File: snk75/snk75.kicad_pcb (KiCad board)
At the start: 2 copper layers, 274 parts, among them J1 USB_C_Receptacle_USB2.0, U1 ATmega32U4-AU, Y1 16MHZ

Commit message: Added PCB rounded borders
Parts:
- D15: moved to F.Cu
- moved R12 471.7 mm to (66.7, 174.4)
- moved R16 471.7 mm to (66.7, 181.0)
- moved R20 471.7 mm to (72.6, 177.7)
- moved R23 471.7 mm to (72.6, 184.3)
- moved R27 471.7 mm to (66.7, 177.7)
- moved R54 471.7 mm to (66.7, 167.8)
- moved R56 471.7 mm to (72.6, 181.0)
- moved R76 471.7 mm to (66.7, 171.1)
- moved R81 471.7 mm to (72.6, 167.8)
- moved R87 471.7 mm to (72.6, 174.4)
- moved R9 471.7 mm to (72.6, 171.1)
- moved R10 410.7 mm to (29.8, 181.3)
- moved R13 410.7 mm to (29.8, 174.7)
- moved R15 410.7 mm to (23.8, 178.0)
- moved R24 410.7 mm to (29.8, 168.2)
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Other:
- board outline added: 314.3 x 123.8 mm

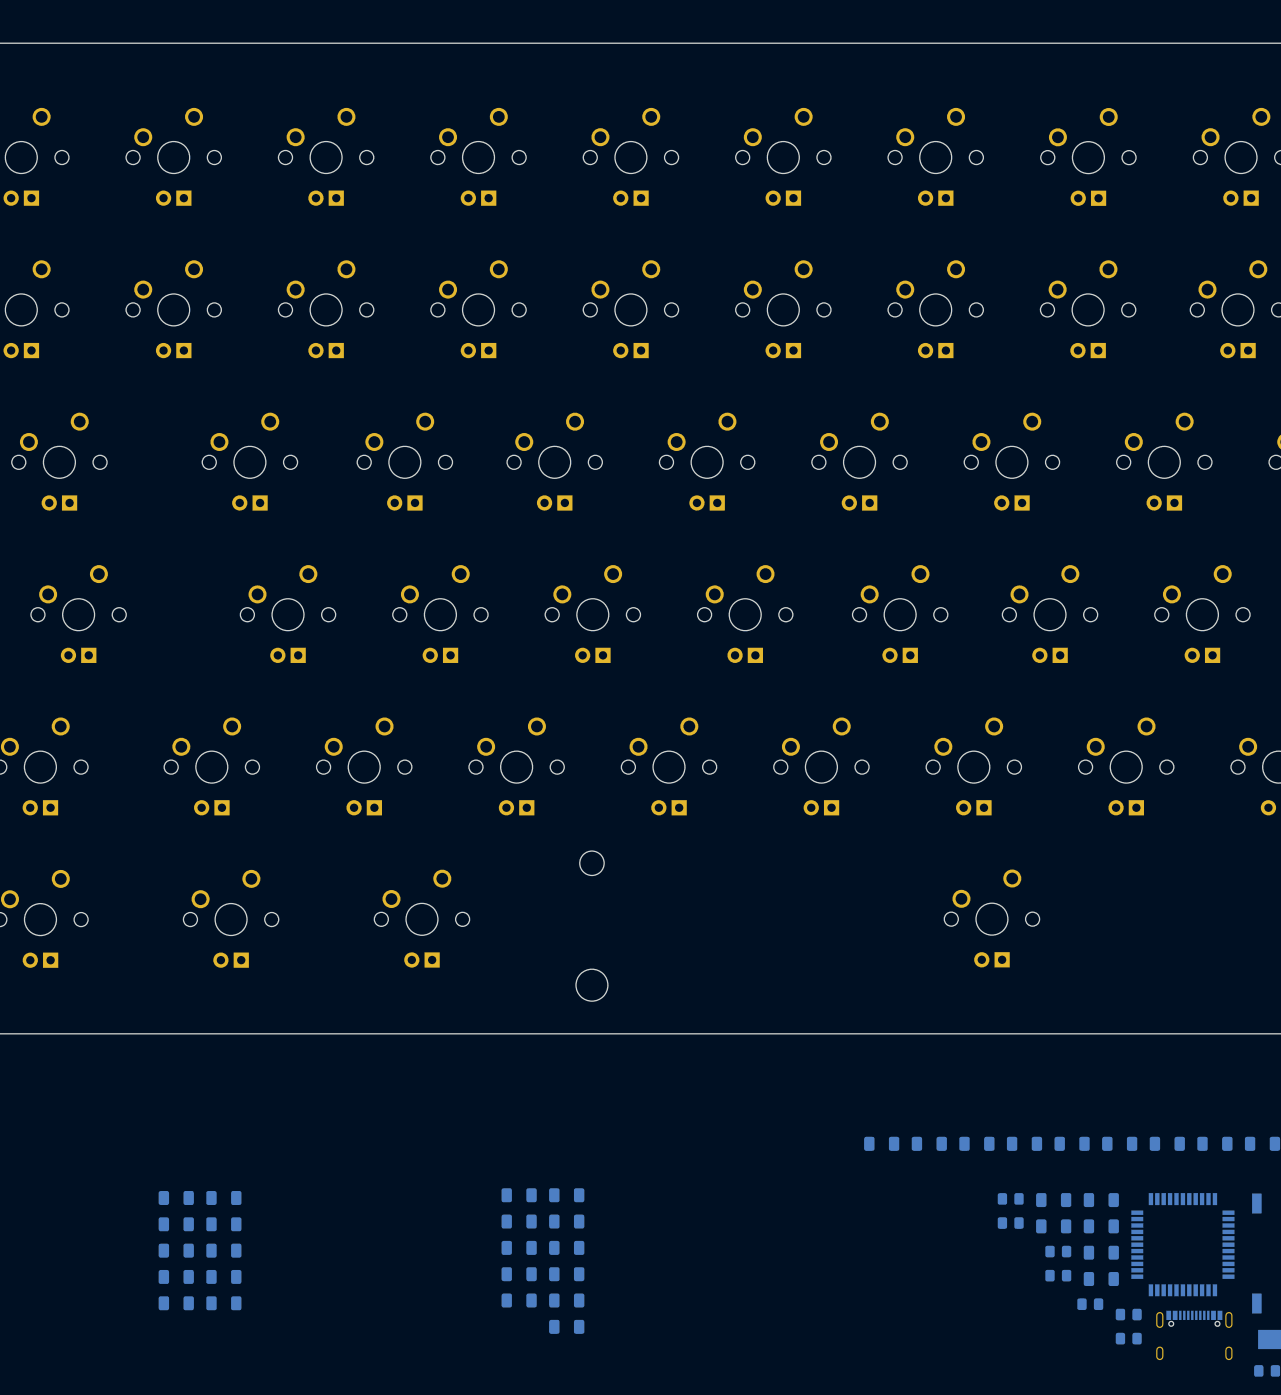
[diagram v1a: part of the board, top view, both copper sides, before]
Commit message: Fixed reset
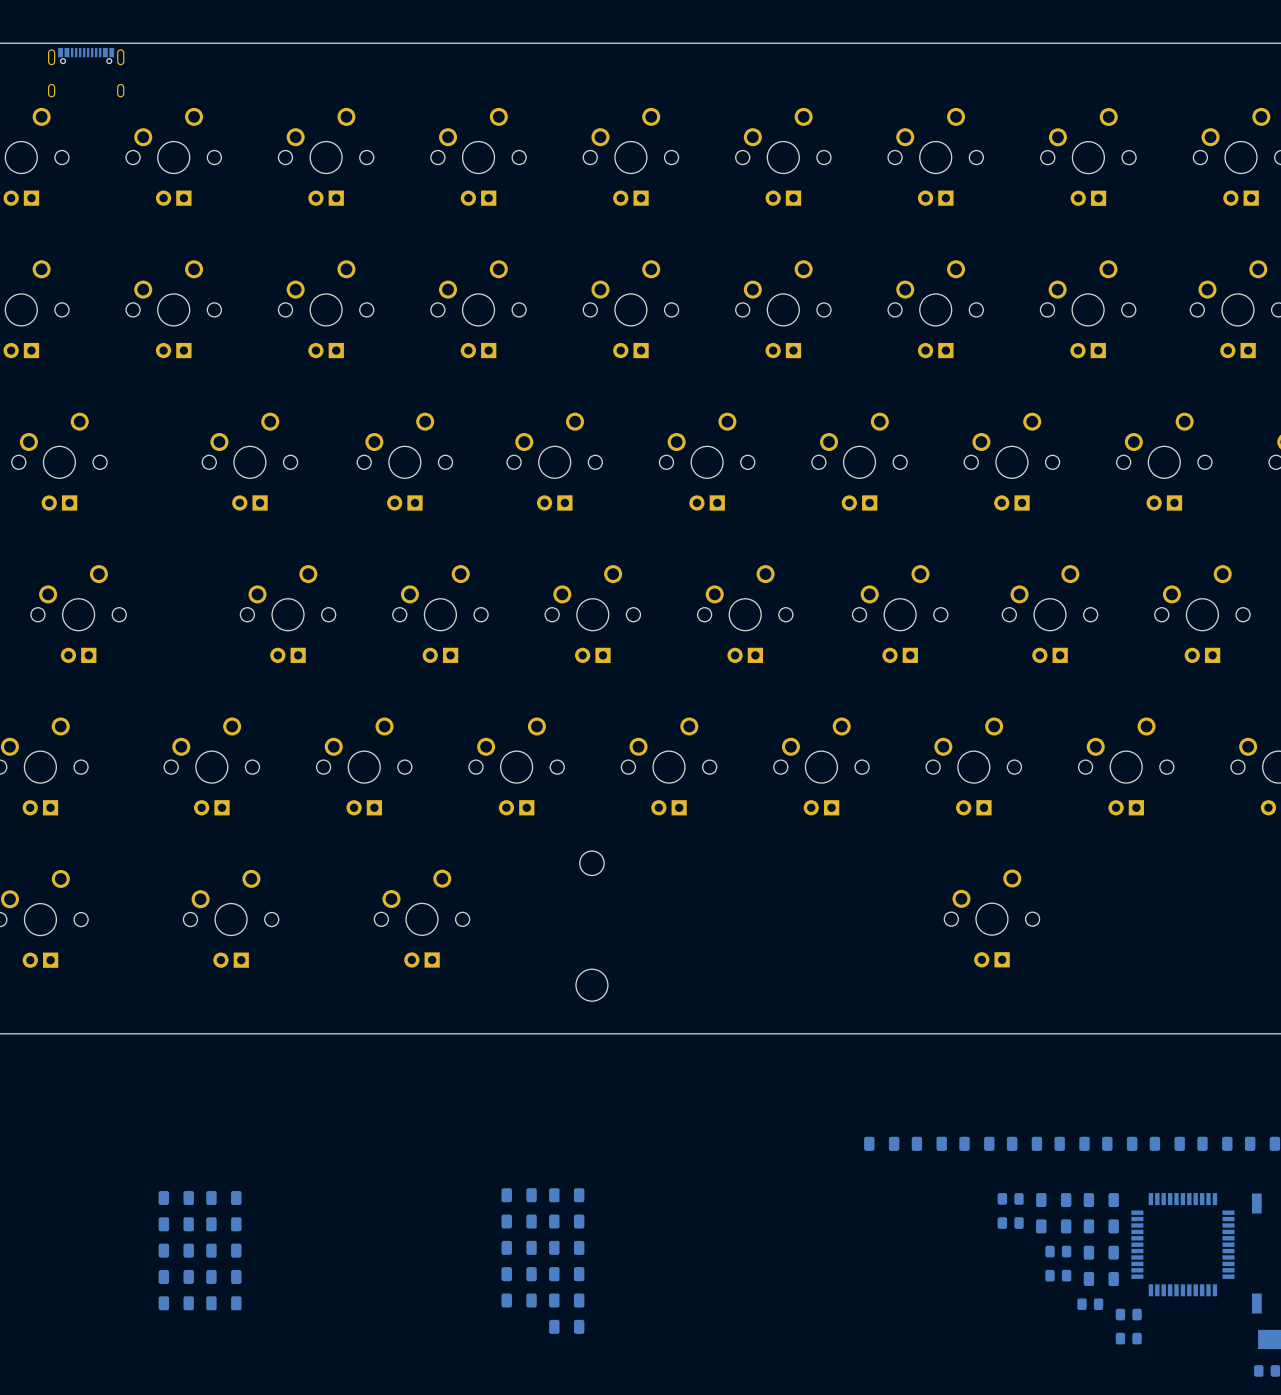
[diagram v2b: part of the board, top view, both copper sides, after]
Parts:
- moved J1 210.0 mm to (12.6, 27.5)
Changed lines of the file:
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@@
   )
   (footprint "Connector_USB:USB_C_Receptacle_Palconn_UTC16-G" (layer "B.Cu")
-    (at 151.075 185.3375 180)
+    (at 12.55 27.5 180)
     (descr "http://www.palpilot.com/wp-content/uploads/2017/05/UTC027-GKN-OR-Rev-A.pdf")
     (tags "USB C Type-C Receptacle USB2.0")

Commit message: Began routing
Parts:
- removed 1uF1: C?, Capacitor_SMD:C_0805_2012Metric_Pad1.18x1.45mm_HandSolder
- added C10: 100n, Capacitor_SMD:C_0805_2012Metric_Pad1.18x1.45mm_HandSolder, B.Cu at (143.8, 138.8)
- added C11: 100nF, Capacitor_SMD:C_0805_2012Metric_Pad1.18x1.45mm_HandSolder, F.Cu at (78.8, -18.6)
- added C12: 100nF, Capacitor_SMD:C_0805_2012Metric_Pad1.18x1.45mm_HandSolder, F.Cu at (101.8, -28.0)
- added C13: 100nF, Capacitor_SMD:C_0805_2012Metric_Pad1.18x1.45mm_HandSolder, F.Cu at (106.7, -37.0)
- added C14: 100nF, Capacitor_SMD:C_0805_2012Metric_Pad1.18x1.45mm_HandSolder, F.Cu at (114.8, -43.1)
- added C15: 100nF, Capacitor_SMD:C_0805_2012Metric_Pad1.18x1.45mm_HandSolder, F.Cu at (101.8, -31.0)
- added C16: 100nF, Capacitor_SMD:C_0805_2012Metric_Pad1.18x1.45mm_HandSolder, F.Cu at (83.6, -18.6)
- added C17: 100nF, Capacitor_SMD:C_0805_2012Metric_Pad1.18x1.45mm_HandSolder, F.Cu at (101.8, -34.0)
- added C18: 100nF, Capacitor_SMD:C_0805_2012Metric_Pad1.18x1.45mm_HandSolder, F.Cu at (74.0, -18.6)
- added C19: 100nF, Capacitor_SMD:C_0805_2012Metric_Pad1.18x1.45mm_HandSolder, F.Cu at (93.7, -21.7)
- added C20: 100nF, Capacitor_SMD:C_0805_2012Metric_Pad1.18x1.45mm_HandSolder, F.Cu at (110.0, -43.1)
- added C21: 100nF, Capacitor_SMD:C_0805_2012Metric_Pad1.18x1.45mm_HandSolder, F.Cu at (69.2, -18.6)
- added C22: 100nF, Capacitor_SMD:C_0805_2012Metric_Pad1.18x1.45mm_HandSolder, F.Cu at (106.7, -34.0)
- added C23: 100nF, Capacitor_SMD:C_0805_2012Metric_Pad1.18x1.45mm_HandSolder, F.Cu at (101.8, -37.0)
- added C24: 100nF, Capacitor_SMD:C_0805_2012Metric_Pad1.18x1.45mm_HandSolder, F.Cu at (93.7, -24.8)
- added C25: 100nF, Capacitor_SMD:C_0805_2012Metric_Pad1.18x1.45mm_HandSolder, F.Cu at (110.0, -40.1)
- added C26: 100nF, Capacitor_SMD:C_0805_2012Metric_Pad1.18x1.45mm_HandSolder, F.Cu at (135.2, 175.0)
- added C27: 100nF, Capacitor_SMD:C_0805_2012Metric_Pad1.18x1.45mm_HandSolder, F.Cu at (135.2, 169.5)
- added C8: 100n, Capacitor_SMD:C_0805_2012Metric_Pad1.18x1.45mm_HandSolder, B.Cu at (148.3, 125.0)
- added C9: 1u, Capacitor_SMD:C_0805_2012Metric_Pad1.18x1.45mm_HandSolder, B.Cu at (143.3, 130.0)
- added D100: SK6812MINI-E, acheron_Components:SK6812MINI_3535_6028_3.2x2.8mm_Round, F.Cu at (87.2, -41.6)
- added D101: SK6812MINI-E, acheron_Components:SK6812MINI_3535_6028_3.2x2.8mm_Round, F.Cu at (70.9, -29.3)
- added D86: SK6812MINI-E, acheron_Components:SK6812MINI_3535_6028_3.2x2.8mm_Round, F.Cu at (79.0, -23.2)
- added D87: SK6812MINI-E, acheron_Components:SK6812MINI_3535_6028_3.2x2.8mm_Round, F.Cu at (79.0, -29.3)
- added D88: SK6812MINI-E, acheron_Components:SK6812MINI_3535_6028_3.2x2.8mm_Round, F.Cu at (70.9, -41.6)
- added D89: SK6812MINI-E, acheron_Components:SK6812MINI_3535_6028_3.2x2.8mm_Round, F.Cu at (87.2, -35.4)
- added D90: SK6812MINI-E, acheron_Components:SK6812MINI_3535_6028_3.2x2.8mm_Round, F.Cu at (79.0, -41.6)
- added D91: SK6812MINI-E, acheron_Components:SK6812MINI_3535_6028_3.2x2.8mm_Round, F.Cu at (103.5, -41.6)
- added D92: SK6812MINI-E, acheron_Components:SK6812MINI_3535_6028_3.2x2.8mm_Round, F.Cu at (95.4, -29.3)
- added D93: SK6812MINI-E, acheron_Components:SK6812MINI_3535_6028_3.2x2.8mm_Round, F.Cu at (70.9, -23.2)
- added D94: SK6812MINI-E, acheron_Components:SK6812MINI_3535_6028_3.2x2.8mm_Round, F.Cu at (87.2, -23.2)
- added D95: SK6812MINI-E, acheron_Components:SK6812MINI_3535_6028_3.2x2.8mm_Round, F.Cu at (79.0, -35.4)
- added D96: SK6812MINI-E, acheron_Components:SK6812MINI_3535_6028_3.2x2.8mm_Round, F.Cu at (95.4, -41.6)
- added D97: SK6812MINI-E, acheron_Components:SK6812MINI_3535_6028_3.2x2.8mm_Round, F.Cu at (70.9, -35.4)
- added D98: SK6812MINI-E, acheron_Components:SK6812MINI_3535_6028_3.2x2.8mm_Round, F.Cu at (87.2, -29.3)
- added D99: SK6812MINI-E, acheron_Components:SK6812MINI_3535_6028_3.2x2.8mm_Round, F.Cu at (95.4, -35.4)
- added FB1: FerriteBead_Small, Inductor_SMD:L_0805_2012Metric, B.Cu at (7.50, 36.5)
- added Q1: AO3400A, Package_TO_SOT_SMD:SOT-23, F.Cu at (210.7, 158.0)
- added U2: USBLC6-2SC6, Package_TO_SOT_SMD:SOT-23-6, B.Cu at (14.1, 45.1)
- C3, D10, D11, D12, D13, D14, D16, D17, D18, D19, D2, D20, D21, D22, D23, D24, D25, D26, D27, D28, D29, D3, D30, D31, D32, D33, D34, D35, D36, D37, D38, D39, D4, D40, D41, D42, D43, D44, D45, D46, D47, D48, D49, D5, D50, D51, D52, D53, D54, D55, D56, D57, D58, D59, D6, D60, D61, D62, D63, D64, D65, D66, D67, D68, D69, D70, D71, D72, D73, D74, D75, D76, D77, D78, D79, D8, D80, D81, D82, D83, D84, D85, D9, R10, R11, R12, R13, R14, R15, R16, R17, R18, R19, R20, R21, R22, R23, R24, R25, R26, R27, R28, R29, R30, R31, R32, R33, R34, R35, R36, R37, R38, R39, R40, R41, R42, R43, R44, R45, R46, R47, R48, R49, R50, R51, R52, R53, R54, R55, R56, R57, R58, R59, R60, R61, R62, R63, R64, R65, R66, R67, R68, R69, R70, R71, R72, R73, R74, R75, R76, R77, R78, R79, R80, R81, R82, R83, R84, R85, R86, R87, R88, R89, R90, R91, R92, SWP1: moved to F.Cu
- C4: value 100n -> 100nF; moved to F.Cu
- C5: value 10uF -> 10u
- C6: value 100n -> 1u
- J1: value USB_C_Receptacle_USB2.0 -> TYPE-C-31-M12_13; footprint Connector_USB:USB_C_Receptacle_Palconn_UTC16-G -> acheron_Connectors:TYPE-C-31-M-12
- R1: value 1k -> 10k; footprint Resistor_SMD:R_1206_3216Metric_Pad1.30x1.75mm_HandSolder -> Resistor_SMD:R_0402_1005Metric; moved to F.Cu
- R2: value 330 -> 100R; footprint Resistor_SMD:R_1206_3216Metric_Pad1.30x1.75mm_HandSolder -> Resistor_SMD:R_0402_1005Metric; moved to F.Cu
- R3: value 22R -> 1k; moved to F.Cu
- R4: value 10k -> 330; moved to F.Cu
- R5: value 22R -> 10k; moved to F.Cu
- moved D7 241.7 mm to (31.5, 38.2), turned to 90 degrees
- moved R8 237.0 mm to (4.70, 45.8)
- moved R7 215.3 mm to (10.9, 40.0), turned to 0 degrees
- moved D15 175.9 mm to (213.8, -46.0)
- moved D42 175.9 mm to (37.9, -201.6), turned to 0 degrees
- moved D62 175.9 mm to (37.9, -194.9), turned to 0 degrees
- moved D69 175.9 mm to (37.9, -198.3), turned to 0 degrees
- moved R34 175.7 mm to (38.0, -204.9), turned to 0 degrees
- moved R36 175.7 mm to (38.0, -208.2), turned to 0 degrees
- moved R6 173.5 mm to (16.8, 40.0)
- moved D26 164.4 mm to (208.1, -46.0), turned to 0 degrees
- moved D34 164.4 mm to (43.7, -201.5), turned to 0 degrees
- moved D21 164.0 mm to (43.9, -204.9), turned to 0 degrees
- moved D43 164.0 mm to (43.9, -208.2), turned to 0 degrees
- moved D50 164.0 mm to (207.9, -42.6), turned to 0 degrees
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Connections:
- net Net-(R10-Pad2) renamed LED-
- C4 pad 2: Net-(C4-Pad2) -> GND
- J1 pad A4: +5V -> VBUS
- J1 pad A6: D+ -> DBUS+
- J1 pad A7: Net-(J1-PadA7) -> DBUS-
- J1 pad B4: +5V -> VBUS
- J1 pad B6: Net-(J1-PadB6) -> DBUS+
- J1 pad B7: D- -> DBUS-
- MX1 pad 4: Net-(MX1-Pad4) -> +5V
- MX10 pad 4: Net-(MX1-Pad4) -> +5V
- MX11 pad 4: Net-(MX1-Pad4) -> +5V
- MX12 pad 4: Net-(MX1-Pad4) -> +5V
- MX13 pad 4: Net-(MX1-Pad4) -> +5V
- MX14 pad 4: Net-(MX1-Pad4) -> +5V
- MX15 pad 4: Net-(MX1-Pad4) -> +5V
- MX16 pad 4: Net-(MX1-Pad4) -> +5V
- MX17 pad 4: Net-(MX1-Pad4) -> +5V
- MX18 pad 4: Net-(MX1-Pad4) -> +5V
- MX19 pad 4: Net-(MX1-Pad4) -> +5V
- MX2 pad 4: Net-(MX1-Pad4) -> +5V
- MX20 pad 4: Net-(MX1-Pad4) -> +5V
- MX21 pad 4: Net-(MX1-Pad4) -> +5V
- MX22 pad 4: Net-(MX1-Pad4) -> +5V
- MX23 pad 4: Net-(MX1-Pad4) -> +5V
- MX24 pad 4: Net-(MX1-Pad4) -> +5V
- MX25 pad 4: Net-(MX1-Pad4) -> +5V
- MX26 pad 4: Net-(MX1-Pad4) -> +5V
- MX27 pad 4: Net-(MX1-Pad4) -> +5V
- MX28 pad 4: Net-(MX1-Pad4) -> +5V
- MX29 pad 4: Net-(MX1-Pad4) -> +5V
- MX3 pad 4: Net-(MX1-Pad4) -> +5V
- MX30 pad 4: Net-(MX1-Pad4) -> +5V
- MX31 pad 4: Net-(MX1-Pad4) -> +5V
- MX32 pad 4: Net-(MX1-Pad4) -> +5V
- MX33 pad 4: Net-(MX1-Pad4) -> +5V
- MX34 pad 4: Net-(MX1-Pad4) -> +5V
- MX35 pad 4: Net-(MX1-Pad4) -> +5V
- MX36 pad 4: Net-(MX1-Pad4) -> +5V
- MX37 pad 4: Net-(MX1-Pad4) -> +5V
- MX38 pad 4: Net-(MX1-Pad4) -> +5V
- MX39 pad 4: Net-(MX1-Pad4) -> +5V
- MX4 pad 4: Net-(MX1-Pad4) -> +5V
- MX40 pad 4: Net-(MX1-Pad4) -> +5V
- MX41 pad 4: Net-(MX1-Pad4) -> +5V
- MX42 pad 4: Net-(MX1-Pad4) -> +5V
- MX43 pad 4: Net-(MX1-Pad4) -> +5V
- MX44 pad 4: Net-(MX1-Pad4) -> +5V
- MX45 pad 4: Net-(MX1-Pad4) -> +5V
- MX46 pad 4: Net-(MX1-Pad4) -> +5V
- MX47 pad 4: Net-(MX1-Pad4) -> +5V
- MX48 pad 4: Net-(MX1-Pad4) -> +5V
- MX49 pad 4: Net-(MX1-Pad4) -> +5V
- MX5 pad 4: Net-(MX1-Pad4) -> +5V
- MX50 pad 4: Net-(MX1-Pad4) -> +5V
- MX51 pad 4: Net-(MX1-Pad4) -> +5V
- MX52 pad 4: Net-(MX1-Pad4) -> +5V
- MX53 pad 4: Net-(MX1-Pad4) -> +5V
- MX54 pad 4: Net-(MX1-Pad4) -> +5V
- MX55 pad 4: Net-(MX1-Pad4) -> +5V
- MX56 pad 4: Net-(MX1-Pad4) -> +5V
- MX57 pad 4: Net-(MX1-Pad4) -> +5V
- MX58 pad 4: Net-(MX1-Pad4) -> +5V
- MX59 pad 4: Net-(MX1-Pad4) -> +5V
- MX6 pad 4: Net-(MX1-Pad4) -> +5V
- MX60 pad 4: Net-(MX1-Pad4) -> +5V
- MX61 pad 4: Net-(MX1-Pad4) -> +5V
- MX62 pad 4: Net-(MX1-Pad4) -> +5V
- MX63 pad 4: Net-(MX1-Pad4) -> +5V
- MX64 pad 4: Net-(MX1-Pad4) -> +5V
- MX65 pad 4: Net-(MX1-Pad4) -> +5V
- MX66 pad 4: Net-(MX1-Pad4) -> +5V
- MX67 pad 4: Net-(MX1-Pad4) -> +5V
- MX68 pad 4: Net-(MX1-Pad4) -> +5V
- MX69 pad 4: Net-(MX1-Pad4) -> +5V
- MX7 pad 4: Net-(MX1-Pad4) -> +5V
- MX70 pad 4: Net-(MX1-Pad4) -> +5V
- MX71 pad 4: Net-(MX1-Pad4) -> +5V
- MX72 pad 4: Net-(MX1-Pad4) -> +5V
- MX73 pad 4: Net-(MX1-Pad4) -> +5V
- MX74 pad 4: Net-(MX1-Pad4) -> +5V
- MX75 pad 4: Net-(MX1-Pad4) -> +5V
- MX76 pad 4: Net-(MX1-Pad4) -> +5V
- MX77 pad 4: Net-(MX1-Pad4) -> +5V
- MX78 pad 4: Net-(MX1-Pad4) -> +5V
- MX79 pad 4: Net-(MX1-Pad4) -> +5V
- MX8 pad 4: Net-(MX1-Pad4) -> +5V
- MX80 pad 4: Net-(MX1-Pad4) -> +5V
- MX81 pad 4: Net-(MX1-Pad4) -> +5V
- MX82 pad 4: Net-(MX1-Pad4) -> +5V
- MX83 pad 4: Net-(MX1-Pad4) -> +5V
- MX84 pad 4: Net-(MX1-Pad4) -> +5V
- MX85 pad 4: Net-(MX1-Pad4) -> +5V
- MX9 pad 4: Net-(MX1-Pad4) -> +5V
- R1 pad 1: GND -> LED_PWM
- R1 pad 2: Net-(R1-Pad2) -> GND
- R2 pad 1: Net-(C4-Pad2) -> LED_PWM
- R2 pad 2: GND -> Net-(Q1-Pad1)
- R3 pad 1: D+ -> GND
- R3 pad 2: Net-(J1-PadB6) -> Net-(R3-Pad2)
- R4 pad 1: RST -> GND
- R4 pad 2: +5V -> Net-(R4-Pad2)
- R5 pad 1: D- -> RST
- R5 pad 2: Net-(J1-PadA7) -> +5V
- SWP1 pad 1: GND -> Net-(R4-Pad2)
- U1 pad 33: Net-(R1-Pad2) -> Net-(R3-Pad2)
- U1 pad 42: unconnected-(U1-Pad42) -> +5V
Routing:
- net D+: track 0.00 -> 203.1 mm
- net D-: track 0.00 -> 203.0 mm
- net +5V: track 0.00 -> 138.8 mm, vias 0 -> 6
- net GND: track 0.00 -> 93.8 mm, vias 0 -> 2
- net row1: track 0.00 -> 39.1 mm
- net VBUS: track 0.00 -> 20.9 mm, vias 0 -> 3
- net DBUS+: track 0.00 -> 18.2 mm, vias 0 -> 2
- net DBUS-: track 0.00 -> 14.5 mm, vias 0 -> 2
- net Net-(D1-Pad2): track 0.00 -> 10.6 mm
- net Net-(J1-PadA5): track 0.00 -> 7.09 mm
- net Net-(C1-Pad2): track 0.00 -> 6.98 mm
- net Net-(D7-Pad2): track 0.00 -> 6.95 mm
- net Net-(C2-Pad2): track 0.00 -> 6.94 mm
- net Net-(J1-PadB5): track 0.00 -> 6.71 mm
- net GNDPWR: track 0.00 -> 3.01 mm

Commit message: Changed MCU for STM32F072C8Tx and wired cols and rows
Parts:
- added U3: 74LVC1G125, Package_TO_SOT_SMD:SOT-23-5_HandSoldering, F.Cu at (93.0, 161.5)
- C1, C10, C26, C27, C5, C6, C7, C8, C9: footprint Capacitor_SMD:C_0805_2012Metric_Pad1.18x1.45mm_HandSolder -> Capacitor_SMD:C_0402_1005Metric
- C11, C12, C13, C14, C15, C16, C17, C18, C19, C20, C21, C22, C23, C24, C25: footprint Capacitor_SMD:C_0805_2012Metric_Pad1.18x1.45mm_HandSolder -> Capacitor_SMD:C_0402_1005Metric; moved to B.Cu
- C2, C3, C4: footprint Capacitor_SMD:C_0805_2012Metric_Pad1.18x1.45mm_HandSolder -> Capacitor_SMD:C_0402_1005Metric_Pad0.74x0.62mm_HandSolder
- D1, D7: footprint Diode_SMD:D_SOD-123 -> acheron_Components:D_SOD-123
- D10, D11, D12, D13, D14, D15, D16, D17, D18, D19, D2, D20, D21, D22, D23, D24, D25, D26, D27, D28, D29, D3, D30, D31, D32, D33, D34, D35, D36, D37, D38, D39, D4, D40, D41, D42, D43, D44, D45, D46, D47, D48, D49, D5, D50, D51, D52, D53, D54, D55, D56, D57, D58, D59, D6, D60, D61, D62, D63, D64, D65, D66, D67, D68, D69, D70, D71, D72, D73, D74, D75, D76, D77, D78, D79, D8, D80, D81, D82, D83, D84, D85, D9: footprint Diode_SMD:D_SOD-123 -> acheron_Components:D_SOD-123; moved to B.Cu
- D100, D101, D86, D87, D88, D89, D90, D91, D92, D93, D94, D95, D96, D97, D98, D99: footprint acheron_Components:SK6812MINI_3535_6028_3.2x2.8mm_Round -> LED_SMD:LED_SK6812MINI_PLCC4_3.5x3.5mm_P1.75mm; moved to B.Cu
- R10, R12, R13, R15, R16, R18, R20, R23, R24, R25, R27, R3, R32, R37, R4, R44, R45, R5, R51, R52, R54, R56, R58, R59, R6, R60, R62, R65, R7, R70, R73, R76, R77, R78, R79, R8, R80, R81, R83, R85, R87, R9: footprint Resistor_SMD:R_1206_3216Metric_Pad1.30x1.75mm_HandSolder -> Resistor_SMD:R_0402_1005Metric
- R11, R14, R17, R19, R21, R22, R26, R28, R29, R30, R31, R33, R34, R35, R36, R38, R39, R40, R41, R42, R43, R46, R47, R48, R49, R50, R53, R55, R57, R61, R63, R64, R66, R67, R68, R69, R71, R72, R74, R75, R82, R84, R86, R88, R89, R90, R91, R92: footprint Resistor_SMD:R_1206_3216Metric_Pad1.30x1.75mm_HandSolder -> Resistor_SMD:R_0402_1005Metric; moved to B.Cu
- U2: footprint Package_TO_SOT_SMD:SOT-23-6 -> acheron_Components:SOT-23-6
- moved R26 321.4 mm to (-63.5, 126.5), turned to 180 degrees
- moved D85 318.3 mm to (298.5, 38.2), turned to 90 degrees
- moved D61 316.9 mm to (-59.1, 106.4), turned to 180 degrees
- moved D72 311.3 mm to (-53.4, 109.7), turned to 180 degrees
- moved D82 311.1 mm to (-53.2, 113.1), turned to 180 degrees
- moved R72 305.9 mm to (-47.5, 106.3), turned to 180 degrees
- moved R84 305.9 mm to (-47.5, 109.6), turned to 180 degrees
- moved D63 305.8 mm to (-47.5, 113.0), turned to 180 degrees
- moved D14 305.6 mm to (-47.2, 116.3), turned to 180 degrees
- moved R39 300.8 mm to (-41.6, 106.3), turned to 180 degrees
- moved R48 300.8 mm to (-41.6, 109.6), turned to 180 degrees
- moved R92 300.8 mm to (-41.6, 112.9), turned to 180 degrees
- moved D36 300.7 mm to (-41.5, 116.2), turned to 180 degrees
- moved D60 300.7 mm to (-41.5, 119.6), turned to 180 degrees
- moved D31 300.6 mm to (-41.3, 123.0), turned to 180 degrees
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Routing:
- net row1: track 39.1 -> 309.0 mm
- net +5V: track 138.8 -> 358.6 mm
- net GND: track 93.8 -> 298.2 mm, vias 2 -> 4
- net Net-(D45-Pad2): track 0.00 -> 7.78 mm
- net Net-(D19-Pad2): track 0.00 -> 7.66 mm
- net Net-(D68-Pad2): track 0.00 -> 7.48 mm
- net Net-(D40-Pad2): track 0.00 -> 7.36 mm
- net Net-(D74-Pad2): track 0.00 -> 7.35 mm
- net Net-(D79-Pad2): track 0.00 -> 7.30 mm
- net Net-(D50-Pad2): track 0.00 -> 7.30 mm
- net Net-(D24-Pad2): track 0.00 -> 7.30 mm
- net Net-(D29-Pad2): track 0.00 -> 7.25 mm
- net Net-(D85-Pad2): track 0.00 -> 7.25 mm
- net Net-(D56-Pad2): track 0.00 -> 7.25 mm
- net Net-(D34-Pad2): track 0.00 -> 7.20 mm
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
